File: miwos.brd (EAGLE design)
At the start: 120 x 120 mm, 44 parts

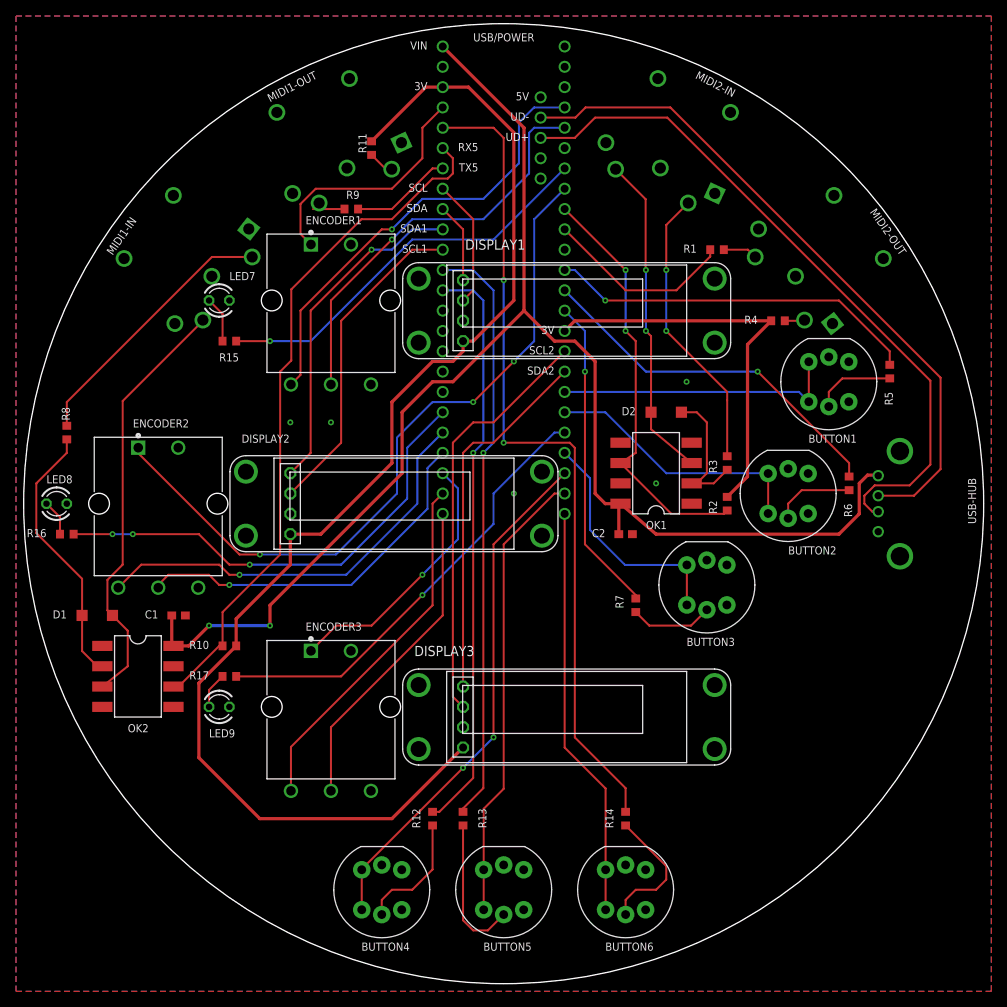
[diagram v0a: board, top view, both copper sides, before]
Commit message: Add shift/menu button
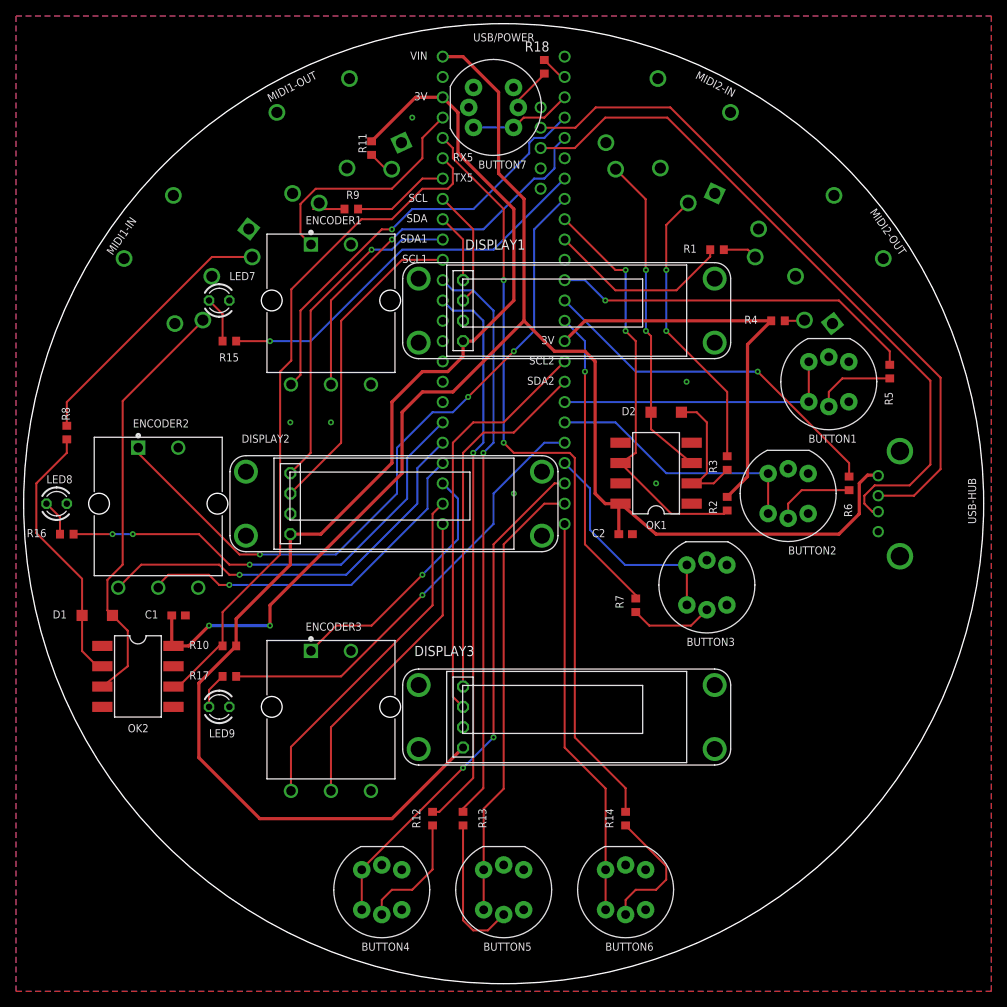
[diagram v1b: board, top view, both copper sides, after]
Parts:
- added BUTTON7: D6RLWHF1LFS, D6RL:D6RL
- added R18: 470R, rcl:R0603
- BUTTON1, BUTTON2, BUTTON3: value D6RL -> D6RLBUF1LFS
- BUTTON4, BUTTON5, BUTTON6: value D6RL -> D6RLGNF1LFS
- R12, R13, R14, R15, R16, R17, R5, R6, R7: value 220R -> 470R
- moved TEENSY-41 1.27 mm to (0.00, 26.7)
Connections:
- removed net RX1: TEENSY-41.0/RX
- removed net TX1: TEENSY-41.1/TX
- new net BUTTON7: BUTTON7.1, BUTTON7.2, TEENSY-41.1/TX
- new net BUTTON7-LED: R18.1, TEENSY-41.0/RX
- new net N$7: BUTTON7.6, R18.2
- net +5V: no longer TEENSY-41.UVHST
- net GND: now also BUTTON7.3, BUTTON7.4, BUTTON7.5
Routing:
- net BUTTON7: track 0.00 -> 13.0 mm
- net BUTTON6-LED: track 103.5 -> 97.8 mm
- net N$7: track 0.00 -> 5.56 mm
- net BUTTON7-LED: track 0.00 -> 3.42 mm
- net +3V3: track 212.3 -> 209.6 mm
- net ENCODER2-PUSH: track 91.2 -> 88.5 mm
- net ENCODER1-A: track 56.2 -> 53.5 mm
- net BUTTON4-LED: track 72.7 -> 70.6 mm
- net ENCODER1-B: track 51.6 -> 49.6 mm
- net BUTTON5-LED: track 74.2 -> 72.2 mm
- net ENCODER1-PUSH: track 30.6 -> 29.3 mm
- net BUTTON6: track 51.6 -> 50.3 mm
- net BUTTON3: track 29.9 -> 28.6 mm
- net SDA: track 9.94 -> 8.67 mm
- net SCL: track 16.1 -> 14.8 mm
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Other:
- board text removed: "5V"
- board text removed: "UD+"
- board text removed: "UD-"

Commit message: Small changes
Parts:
- moved R8 6.84 mm to (-48.3, 11.4)
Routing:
- net N$10: track 33.6 -> 28.5 mm
- net N$8: track 33.7 -> 34.3 mm
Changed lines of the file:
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@@
 <attribute name="PURCHASE-URL" value="https://pricing.snapeda.com/search/part/57PC5FS/?ref=eda" x="-71.79615" y="63.7723875" size="1.778" layer="28" rot="MR245" display="off"/>
 </element>
-<element name="R8" library="rcl" library_urn="urn:adsk.eagle:library:334" package="R0603" package3d_urn="urn:adsk.eagle:package:23555/3" value="220R" x="-54.61" y="8.89" smashed="yes" rot="R270">
-<attribute name="NAME" x="-55.245" y="12.065" size="1.016" layer="25" font="vector" ratio="12" rot="R270"/>
-<attribute name="POPULARITY" value="70" x="-16.51" y="52.07" size="1.778" layer="27" rot="R270" display="off"/>
-<attribute name="SPICEPREFIX" value="R" x="-16.51" y="52.07" size="1.778" layer="27" rot="R270" display="off"/>
+<element name="R8" library="rcl" library_urn="urn:adsk.eagle:library:334" package="R0603" package3d_urn="urn:adsk.eagle:package:23555/3" value="220R" x="-48.26" y="11.43" smashed="yes" rot="R270">
+<attribute name="NAME" x="-48.895" y="14.605" size="1.016" layer="25" font="vector" ratio="12" rot="R270"/>
+<attribute name="POPULARITY" value="70" x="-10.16" y="54.61" size="1.778" layer="27" rot="R270" display="off"/>
+<attribute name="SPICEPREFIX" value="R" x="-10.16" y="54.61" size="1.778" layer="27" rot="R270" display="off"/>
 </element>
 <element name="D1" library="diode" library_urn="urn:adsk.eagle:library:210" package="SOD123" package3d_urn="urn:adsk.eagle:package:43420/1" value="" x="-50.8" y="-13.97" smashed="yes">
@@
 <wire x1="-52.705" y1="-18.415" x2="-50.8" y2="-20.32" width="0.254" layer="1"/>
 <wire x1="-50.8" y1="-20.32" x2="-50.165" y2="-20.32" width="0.254" layer="1"/>
-<wire x1="-52.7" y1="-13.97" x2="-52.7" y2="-9.388346875" width="0.254" layer="1"/>
-<wire x1="-52.7" y1="-9.388346875" x2="-58.42" y2="-3.668346875" width="0.254" layer="1"/>
-<wire x1="-58.42" y1="-3.668346875" x2="-58.42" y2="2.54" width="0.254" layer="1"/>
-<wire x1="-54.61" y1="6.35" x2="-54.61" y2="8.04" width="0.254" layer="1"/>
-<wire x1="-58.42" y1="2.54" x2="-54.61" y2="6.35" width="0.254" layer="1"/>
+<wire x1="-52.7" y1="-13.97" x2="-52.7" y2="-10.79" width="0.254" layer="1"/>
+<wire x1="-48.137" y1="-6.227" x2="-48.137" y2="10.457" width="0.254" layer="1"/>
+<wire x1="-48.137" y1="10.457" x2="-48.26" y2="10.58" width="0.254" layer="1"/>
+<wire x1="-52.7" y1="-10.79" x2="-48.137" y2="-6.227" width="0.254" layer="1"/>
 </signal>
 <signal name="N$9">
@@
 <contactref element="MIDI1-IN" pad="5"/>
 <contactref element="D1" pad="A"/>
-<wire x1="-37.60170625" y1="22.94974375" x2="-37.60170625" y2="22.86" width="0.254" layer="1"/>
+<wire x1="-37.60170625" y1="22.86" x2="-37.60170625" y2="22.94974375" width="0.254" layer="1"/>
 <wire x1="-50.165" y1="-22.86" x2="-46.99" y2="-20.32" width="0.254" layer="1"/>
 <wire x1="-46.99" y1="-15.88" x2="-48.9" y2="-13.97" width="0.254" layer="1"/>
@@
 <wire x1="-48.9" y1="-13.97" x2="-49.53" y2="-13.34" width="0.254" layer="1"/>
 <wire x1="-49.53" y1="-13.34" x2="-49.53" y2="-9.525" width="0.254" layer="1"/>
-<wire x1="-47.625" y1="12.83670625" x2="-37.60170625" y2="22.86" width="0.254" layer="1"/>
-<wire x1="-47.625" y1="-7.62" x2="-47.625" y2="12.83670625" width="0.254" layer="1"/>
-<wire x1="-49.53" y1="-9.525" x2="-47.625" y2="-7.62" width="0.254" layer="1"/>
+<wire x1="-46.99" y1="13.47170625" x2="-37.60170625" y2="22.86" width="0.254" layer="1"/>
+<wire x1="-46.99" y1="-6.985" x2="-46.99" y2="13.47170625" width="0.254" layer="1"/>
+<wire x1="-49.53" y1="-9.525" x2="-46.99" y2="-6.985" width="0.254" layer="1"/>
 </signal>
 <signal name="N$10">
 <contactref element="MIDI1-IN" pad="4"/>
 <contactref element="R8" pad="1"/>
-<wire x1="-54.61" y1="9.74" x2="-54.61" y2="12.7" width="0.254" layer="1"/>
-<wire x1="-36.47226875" y1="30.83773125" x2="-54.61" y2="12.7" width="0.254" layer="1"/>
-<wire x1="-36.47226875" y1="30.83773125" x2="-31.438934375" y2="30.83773125" width="0.254" layer="1"/>
+<wire x1="-48.26" y1="12.28" x2="-48.26" y2="13.97" width="0.254" layer="1"/>
+<wire x1="-43.18" y1="19.05" x2="-48.26" y2="13.97" width="0.254" layer="1"/>
+<wire x1="-31.438934375" y1="30.83773125" x2="-36.47226875" y2="30.83773125" width="0.254" layer="1"/>
+<wire x1="-36.47226875" y1="30.83773125" x2="-43.18" y2="24.13" width="0.254" layer="1"/>
+<wire x1="-43.18" y1="24.13" x2="-43.18" y2="19.05" width="0.254" layer="1"/>
 </signal>
 <signal name="N$11">
@@
 <via x="-31.75" y="-7.62" extent="1-16" drill="0.35"/>
 <wire x1="-31.75" y1="-7.62" x2="-34.29" y2="-7.62" width="0.254" layer="1"/>
-<wire x1="-53.76" y1="-3.81" x2="-48.895" y2="-3.81" width="0.254" layer="1"/>
-<via x="-48.895" y="-3.81" extent="1-16" drill="0.35"/>
-<wire x1="-48.895" y1="-3.81" x2="-46.355" y2="-3.81" width="0.254" layer="16"/>
-<via x="-46.355" y="-3.81" extent="1-16" drill="0.35"/>
-<wire x1="-46.355" y1="-3.81" x2="-38.1" y2="-3.81" width="0.254" layer="1"/>
+<wire x1="-53.76" y1="-3.81" x2="-50.165" y2="-3.81" width="0.254" layer="1"/>
+<via x="-50.165" y="-3.81" extent="1-16" drill="0.35"/>
+<wire x1="-50.165" y1="-3.81" x2="-45.085" y2="-3.81" width="0.254" layer="16"/>
+<via x="-45.085" y="-3.81" extent="1-16" drill="0.35"/>
+<wire x1="-45.085" y1="-3.81" x2="-38.1" y2="-3.81" width="0.254" layer="1"/>
 </signal>
 <signal name="ENCODER3-LED">

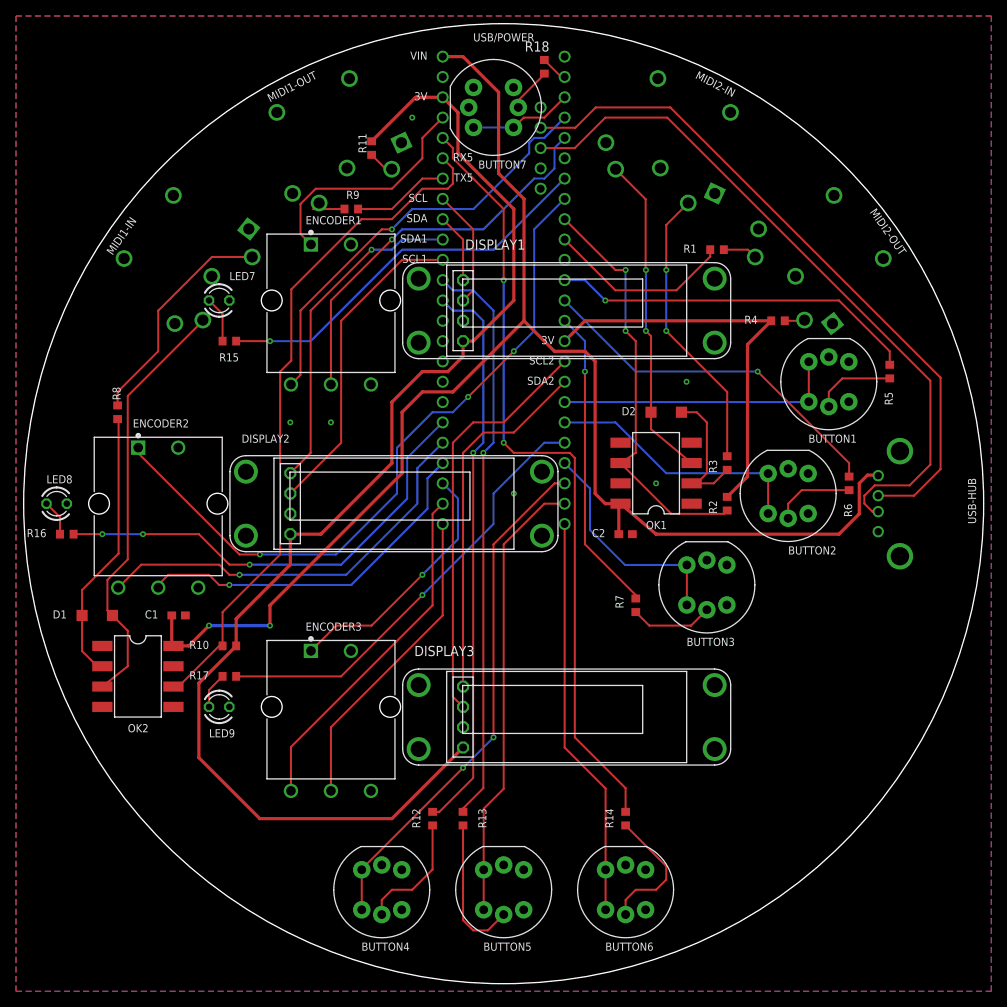
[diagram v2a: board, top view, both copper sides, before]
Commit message: Use non-illuminated buttons, add mounting holes
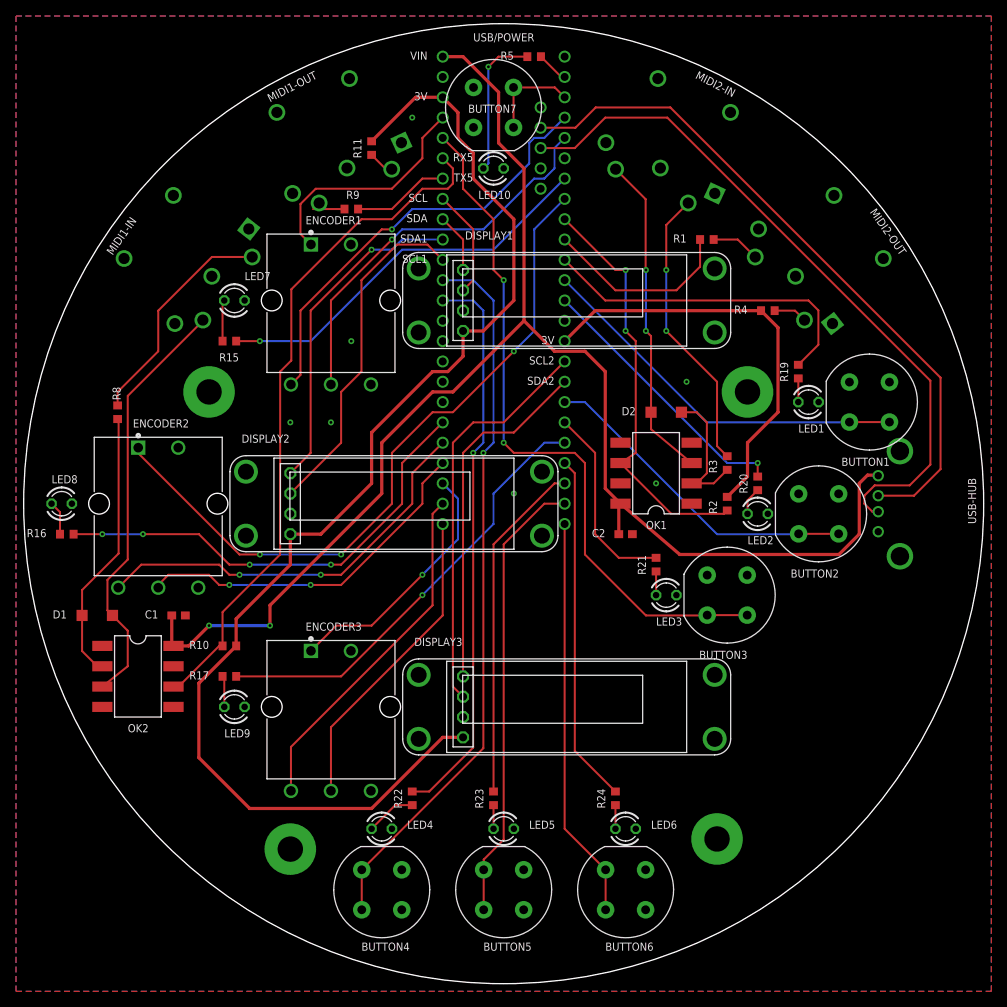
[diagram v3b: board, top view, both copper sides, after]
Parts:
- removed R12, R13, R14, R18, R6, R7: 470R, rcl:R0603
- added LED1, LED10, LED2, LED3, LED4, LED5, LED6: (no value), led:LED3MM
- added P1, P2, P3, P4: MOUNT_CH, sol_pin:MOUNT_CH32
- added R19, R20, R21, R22, R23, R24: 470R, rcl:R0603
- BUTTON1, BUTTON2, BUTTON3: value D6RLBUF1LFS -> D6R60F1LFS; device D6RL:D6RL -> D6R:D6R
- BUTTON4, BUTTON5, BUTTON6: value D6RLGNF1LFS -> D6R60F1LFS; device D6RL:D6RL -> D6R:D6R
- BUTTON7: value D6RLWHF1LFS -> D6R60F1LFS; device D6RL:D6RL -> D6R:D6R
- OK1, OK2: device 6N138:DIL08 -> 6N138:DIP08-SMD
- moved R5 59.4 mm to (3.81, 55.9), turned to 180 degrees
- moved BUTTON1 5.68 mm to (45.7, 12.7), turned to 90 degrees
- moved BUTTON2 4.58 mm to (39.4, -1.27), turned to 90 degrees
- moved BUTTON3 2.84 mm to (27.9, -11.4), turned to 90 degrees
- moved LED7 1.91 mm to (-33.7, 25.4)
- moved LED9 1.91 mm to (-33.7, -25.4)
- moved R1 1.80 mm to (25.4, 33.0)
- moved R4 1.80 mm to (33.0, 24.1)
- moved DISPLAY3 1.27 mm to (7.87, -25.4)
- moved DISPLAY1 1.27 mm to (7.87, 25.4)
- moved LED8 0.64 mm to (-55.2, 0.00)
- turned BUTTON7 to 180 degrees
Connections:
- removed net N$1: TEENSY-41.39
- removed net N$13: BUTTON4.6, R12.2
- removed net N$14: BUTTON1.6, R5.2
- removed net N$15: BUTTON6.6, R14.2
- removed net N$23: BUTTON5.6, R13.2
- removed net N$6: BUTTON2.6, R6.2
- removed net N$7: BUTTON7.6, R18.2
- new net N$25: LED1.A, R19.2
- new net N$27: LED2.A, R20.2
- new net N$29: LED3.A, R21.2
- new net N$31: LED4.A, R22.2
- new net N$33: LED5.A, R23.2
- new net N$35: LED6.A, R24.2
- net BUTTON1: now also TEENSY-41.10/CS; no longer TEENSY-41.26
- net BUTTON1-LED: now also R19.1, TEENSY-41.9; no longer R5.1, TEENSY-41.10/CS
- net BUTTON2: now also TEENSY-41.26; no longer TEENSY-41.27
- net BUTTON2-LED: now also R20.1; no longer R6.1
- net BUTTON3: now also TEENSY-41.22/A8; no longer TEENSY-41.29
- net BUTTON3-LED: now also R21.1, TEENSY-41.27; no longer R7.1, TEENSY-41.12/MISO
- net BUTTON4: now also TEENSY-41.15/A1; no longer TEENSY-41.30
- net BUTTON4-LED: now also R22.1; no longer R12.1
- net BUTTON5-LED: now also R23.1, TEENSY-41.30; no longer R13.1, TEENSY-41.15/A1
- net BUTTON6-LED: now also R24.1, TEENSY-41.29; no longer R14.1, TEENSY-41.22/A8
- net BUTTON7-LED: now also R5.1; no longer R18.1
- net GND: now also LED1.K, LED10.K, LED2.K, LED3.K, LED4.K, LED5.K, LED6.K; no longer BUTTON1.5, BUTTON2.5, BUTTON3.5, BUTTON4.5, BUTTON5.5, BUTTON6.5, BUTTON7.5
- net N$5: now also LED10.A, R5.2; no longer BUTTON3.6, R7.2
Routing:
- net BUTTON3: track 28.6 -> 87.4 mm, vias 0 -> 2
- net BUTTON6-LED: track 97.8 -> 43.7 mm, vias 2 -> 0
- net BUTTON5-LED: track 72.2 -> 42.9 mm, vias 1 -> 0
- net BUTTON4: track 64.5 -> 90.4 mm, vias 2 -> 1
- net N$23: track 18.3 -> 0.00 mm
- net N$15: track 16.8 -> 0.00 mm
- net N$13: track 15.3 -> 0.00 mm
- net BUTTON3-LED: track 38.4 -> 24.4 mm, vias 1 -> 0
- net BUTTON1: track 35.6 -> 48.0 mm
- net BUTTON2-LED: track 45.7 -> 34.2 mm
- net N$6: track 10.2 -> 0.00 mm
- net N$14: track 10.2 -> 0.00 mm
- net BUTTON2: track 33.1 -> 41.1 mm
- net N$5: track 10.4 -> 18.4 mm, vias 0 -> 1
- net N$31: track 0.00 -> 6.31 mm
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
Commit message: Various changes
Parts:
- removed LED7, LED8, LED9: (no value), led:LED3MM
- removed R15, R16, R17: 470R, rcl:R0603
- ENCODER2: value PEC16 -> PEC11R-4215F-S0024; device PEC16:PEC16 -> PEC11R-4215F-S0024:XDCR_PEC11R-4215F-S0024
- moved ENCODER2 1.27 mm to (-44.5, 0.00), turned to 0 degrees
- moved P4 1.14 mm to (30.0, 15.0)
- moved P1 0.38 mm to (-27.0, -43.0)
- moved P2 0.34 mm to (27.0, -42.0)
- moved P3 0.17 mm to (-37.0, 14.0)
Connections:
- removed net ENCODER1-LED: R15.1, TEENSY-41.5
- removed net ENCODER2-LED: R16.1, TEENSY-41.38
- removed net ENCODER3-LED: R17.1, TEENSY-41.28
- removed net N$20: LED8.A, R16.2
- removed net N$22: LED9.A, R17.2
- removed net N$4: LED7.A, R15.2
- net GND: now also ENCODER2.COM; no longer ENCODER2.C, LED7.K, LED8.K, LED9.K
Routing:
- net ENCODER2-LED: track 58.1 -> 0.00 mm, vias 4 -> 0
- net ENCODER3-LED: track 55.4 -> 0.00 mm, vias 1 -> 0
- net ENCODER1-LED: track 49.5 -> 0.00 mm, vias 1 -> 0
- net N$4: track 5.17 -> 0.00 mm
- net N$20: track 4.25 -> 0.00 mm
- net N$22: track 3.90 -> 0.00 mm
- net ENCODER2-PUSH: track 88.8 -> 92.3 mm
- net N$9: track 53.3 -> 56.5 mm
- net ENCODER2-B: track 44.8 -> 43.2 mm
- net N$8: track 34.3 -> 35.7 mm

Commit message: Use TRS midi
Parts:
- removed P1, P2, P3, P4: MOUNT_CH, sol_pin:MOUNT_CH32
- ENCODER2: value PEC11R-4215F-S0024 -> PEC16; device PEC11R-4215F-S0024:XDCR_PEC11R-4215F-S0024 -> PEC16:PEC16
- MIDI1-IN, MIDI1-OUT, MIDI2-IN, MIDI2-OUT: value ADAFRUIT-5PIN-DIN -> 35RASMT2BHNTRX; device adafruit-5pin-din:ADAFRUIT-5PIN-DIN -> 35RASMT2BHNTRX:SWITCHCRAFT_35RASMT2BHNTRX
- moved D1 45.6 mm to (-40.6, 30.5)
- moved C1 44.9 mm to (-34.3, 30.5)
- moved OK2 44.7 mm to (-40.6, 22.9)
- moved R10 36.9 mm to (-33.0, 19.1), turned to 90 degrees
- moved R8 23.3 mm to (-39.4, 33.0), turned to 180 degrees
- moved R2 22.5 mm to (12.7, 16.5)
- moved MIDI1-IN 16.8 mm to (-27.5, 42.2), flipped to the top, turned to 303 degrees
- moved MIDI2-OUT 16.8 mm to (27.5, 42.2), flipped to the top, turned to 237 degrees
- moved R4 11.7 mm to (30.5, 35.6)
- moved R20 10.2 mm to (30.5, 12.7)
- moved R21 8.52 mm to (11.4, -3.81)
- moved R1 7.73 mm to (17.8, 34.3), turned to 270 degrees
- moved R11 7.18 mm to (-11.4, 49.5), turned to 270 degrees
- moved BUTTON1 6.87 mm to (41.9, 18.4)
- moved BUTTON3 6.87 mm to (24.1, -5.71)
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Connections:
- net GND: now also ENCODER2.C, MIDI1-OUT.5, MIDI2-OUT.5; no longer ENCODER2.COM, MIDI1-IN.G1, MIDI1-IN.G2, MIDI1-OUT.2, MIDI1-OUT.G1, MIDI1-OUT.G2, MIDI2-IN.G1, MIDI2-IN.G2, MIDI2-OUT.2, MIDI2-OUT.G1, MIDI2-OUT.G2
- net N$10: now also MIDI1-IN.1; no longer MIDI1-IN.4
- net N$11: now also MIDI1-OUT.4; no longer MIDI1-OUT.5
- net N$12: now also MIDI1-OUT.1; no longer MIDI1-OUT.4
- net N$17: now also MIDI2-IN.4; no longer MIDI2-IN.5
- net N$18: now also MIDI2-IN.1; no longer MIDI2-IN.4
- net N$19: now also MIDI2-OUT.4; no longer MIDI2-OUT.5
- net N$21: now also MIDI2-OUT.1; no longer MIDI2-OUT.4
- net N$9: now also MIDI1-IN.4; no longer MIDI1-IN.5
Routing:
- net RX5: track 85.7 -> 44.0 mm
- net N$9: track 56.5 -> 24.7 mm
- net +3V3: track 210.8 -> 180.7 mm, vias 0 -> 1
- net N$8: track 35.7 -> 11.2 mm
- net RX2: track 52.1 -> 33.9 mm, vias 2 -> 1
- net BUTTON1-LED: track 42.2 -> 26.4 mm
- net TX2: track 24.2 -> 11.4 mm
- net BUTTON3-LED: track 24.4 -> 12.9 mm
- net N$18: track 35.9 -> 46.6 mm
- net BUTTON3: track 87.4 -> 77.9 mm
- net N$10: track 28.5 -> 19.0 mm
- net SCL1: track 43.1 -> 34.6 mm
- net BUTTON2-LED: track 34.2 -> 26.7 mm, vias 1 -> 0
- net BUTTON1: track 48.0 -> 40.7 mm
- net ENCODER3-PUSH: track 31.9 -> 25.2 mm, vias 1 -> 0
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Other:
- board size 120 x 120 mm -> 115 x 115 mm
- board text removed: "MIDI1-IN"
- board text removed: "MIDI1-OUT"
- board text removed: "MIDI2-IN"
- board text removed: "MIDI2-OUT"
- board text removed: "RX5"
- board text removed: "SCL"
- board text removed: "SCL1"
- board text removed: "SDA"
- board text removed: "SDA1"
- board text removed: "TX5"
- board text removed: "USB/POWER"
